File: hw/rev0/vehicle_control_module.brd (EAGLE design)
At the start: 160 x 100 mm, 455 parts, among them IC1 SJA1105TELY, IC10 TJA1100HNZ, IC11 KSZ8061MNXI-TR, IC12 TJA1100HNZ, IC14 NUP2202W1T2G, IC15 TLE9252VSKXUMA1, IC16 NUP2202W1T2G, IC17 LP5907QMFX-3.3Q1, IC2 ATSAMV71Q21B-AABT, IC3 TJA1100HNZ, IC4 FT2232HL, IC5 TRS3232EQPWRQ1, IC6 SST26VF032BT-104I_SM, IC7 DS3231SN#, IC8 TLE9252VSKXUMA1, IC9 TPS62242DRVR, J10 5-2337992-3, J11 2301843-1, J12 1017505, J13 2301843-1, J15 693022010811, J2 2305018-2, J27 2041119-2, J3 1017505, J4 1017505, J5 1017505, J6 1017505, J7 1017505, J8 1017505, J9 1017505, U1 122-2920-GR, U2 LM63625, U3 TPS62007-Q1_DGS_10, Y1 NX3225SA-25MHZ-EXS00A-CS11338, Y2 NX2016SA-25.000M-STD-CZS-1, Y3 ABM8AIG-12.000MHZ-1Z-T

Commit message: Swap to simple CAN transciever, no wake on CAN functionality required
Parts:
- removed IC15, IC8: TLE9252VSKXUMA1, samacsys:SOIC127P599X173-14N
- added C146, C147: 100nF, rcl:C0603
- added IC13, IC18: TLE9250XSJXUMA1, samacsys:SOIC127P602X173-8N
- added R195, R196: 10k, rcl:R0603
- C92, C95: value 100nF -> 10uF
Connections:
- removed net CAN0_EN: IC2.37, IC8.6
- removed net CAN0_ERR: IC2.39, IC8.8
- removed net CAN0_STBY: IC2.38, IC8.14
- removed net CAN1_EN: IC15.6, IC2.94
- removed net CAN1_ERR: IC15.8, IC2.90
- removed net CAN1_STBY: IC15.14, IC2.93
- new net CAN0_RW_MODE: IC13.8, IC2.35, R196.2
- new net CAN1_RW_MODE: IC18.8, IC2.93, R195.2
- net +3V3: now also C146.1, C147.1, IC13.5, IC18.5, R195.1, R196.1; no longer C91.1, C92.1, C94.1, C95.1, IC15.3, IC15.5, IC8.3, IC8.5
- net +5V: now also C91.1, C92.1, C94.1, C95.1, IC13.3, IC18.3
- net CAN0_H: now also IC13.7; no longer IC8.13
- net CAN0_L: now also IC13.6; no longer IC8.12
- net CAN0_RX: now also IC13.4; no longer IC8.4
- net CAN0_TX: now also IC13.1; no longer IC8.1
- net CAN1_H: now also IC18.7; no longer IC15.13
- net CAN1_L: now also IC18.6; no longer IC15.12
- net CAN1_RX: now also IC18.4; no longer IC15.4
- net CAN1_TX: now also IC18.1; no longer IC15.1
- net GND: now also C146.2, C147.2, IC13.2, IC18.2; no longer IC15.2, IC8.2
- net VBATT_PROT: no longer IC15.10, IC15.9, IC8.10, IC8.9

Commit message: Add digital inputs, connect MCU power supply
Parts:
- removed C30, C31: 8pF, rcl:C0603
- removed IC14, IC16: NUP2202W1T2G, samacsys:SOT65P210X110-6N
- removed R183, R188, R193: 1k, rcl:R0603
- removed Y2: NX2016SA-25.000M-STD-CZS-1, samacsys:NX2016SA32MEXS00ACS06465
- added C148, C149, C150, C151, C152, C153, C154, C155: 0.01uF, rcl:C0603
- added C156, C157, C158, C159, C160, C161, C163, C164, C166, C167, C168, C169, C170, C171, C172: 100nF, rcl:C0603
- added C162: 1uF, rcl:C0603
- added C165: 4.7uF, rcl:C0603
- added D28, D29, D30, D31, D32, D33, D34, D35: BAT54SWFILMY, samacsys:SOT65P210X110-3N
- added IC8: 74HC7541D-Q100J, samacsys:SOIC127P1032X265-20N
- added R198: 4.7k, rcl:R0603
- R109, R118, R128, R138, R148, R158, R168, R178: value 1k -> 100k
- R113, R123, R133, R143, R153, R163, R173: value 1k -> 4.7k
- moved R113 315.0 mm to (-294.6, 749.3)
- moved R118 283.4 mm to (-288.3, 749.3)
- moved R123 266.5 mm to (-294.6, 763.3)
- moved R128 234.2 mm to (-288.3, 763.3)
- moved R148 209.8 mm to (-280.7, 791.2)
- moved R143 207.3 mm to (-287.0, 791.2)
- moved R133 201.4 mm to (-294.6, 777.2)
- moved R138 191.2 mm to (-288.3, 777.2)
- moved R178 157.7 mm to (-288.3, 801.4)
- moved R158 154.6 mm to (-288.3, 796.3)
- moved R173 151.6 mm to (-294.6, 801.4)
- moved R153 148.9 mm to (-294.6, 796.3)
- moved R168 134.0 mm to (-275.6, 796.3)
- moved R163 131.8 mm to (-281.9, 796.3)
- moved R109 71.2 mm to (-294.6, -1394.5)
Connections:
- removed net N$22: C31.1, IC11.1, Y2.3
- removed net N$23: C30.1, IC11.2, Y2.1
- new net EXT_DINPUT_0: R198.1
- new net EXT_DINPUT_1: R113.1
- new net EXT_DINPUT_2: R123.1
- new net EXT_DINPUT_3: R133.1
- new net EXT_DINPUT_4: R143.1
- new net EXT_DINPUT_5: R153.1
- new net EXT_DINPUT_6: R163.1
- new net EXT_DINPUT_7: R173.1
- new net INTREG_1V2: C156.1, C157.1, C158.1, C159.1, C160.1, C161.1, C162.1, C163.1, C164.1, IC2.107, IC2.123, IC2.139, IC2.29, IC2.3, IC2.33, IC2.50, IC2.81
- new net N$148: C148.1, D29.3, IC8.3, R113.2, R118.2
- new net N$149: C149.1, D30.3, IC8.4, R123.2, R128.2
- new net N$150: C150.1, D31.3, IC8.5, R133.2, R138.2
- new net N$151: C151.1, D28.3, IC8.2, R109.2, R198.2
- new net N$152: C152.1, D32.3, IC8.6, R143.2, R148.2
- new net N$153: C153.1, D33.3, IC8.7, R153.2, R158.2
- new net N$154: C154.1, D34.3, IC8.8, R163.2, R168.2
- new net N$155: C155.1, D35.3, IC8.9, R173.2, R178.2
- new net PROT_DINPUT_0: IC2.108, IC8.18
- new net PROT_DINPUT_1: IC2.106, IC8.17
- new net PROT_DINPUT_2: IC2.103, IC8.16
- new net PROT_DINPUT_3: IC2.101, IC8.15
- new net PROT_DINPUT_4: IC2.100, IC8.14
- new net PROT_DINPUT_5: IC2.99, IC8.13
- new net PROT_DINPUT_6: IC2.97, IC8.12
- new net PROT_DINPUT_7: IC2.94, IC8.11
- new net SWITCH_REF_CLK: IC1.H1, IC11.1
- net +3V3: now also C165.1, C166.1, C167.1, C168.1, C169.1, C170.1, C171.1, C172.1, D28.1, D29.1, D30.1, D31.1, D32.1, D33.1, D34.1, D35.1, IC1.D10, IC1.D11, IC1.D4, IC1.D5, IC1.D7, IC1.D8, IC1.E11, IC1.E4, IC1.G11, IC1.G4, IC1.H4, IC1.K11, IC1.L10, IC1.L11, IC1.L5, IC1.L8, IC2.134, IC2.143, IC2.30, IC2.43, IC2.5, IC2.72, IC2.80, IC2.96, IC8.20; no longer IC14.5, IC16.5
- net 3V3_AD_REF: now also IC2.9
- net CAN0_H: no longer IC14.1
- net CAN0_L: no longer IC14.6
- net CAN0_RW_MODE: now also IC2.37; no longer IC2.35
- net CAN1_H: no longer IC16.1
- net CAN1_L: no longer IC16.6
- net CAN1_RW_MODE: now also IC2.90; no longer IC2.93
- net GND: now also C148.2, C149.2, C150.2, C151.2, C152.2, C153.2, C154.2, C155.2, C156.2, C157.2, C158.2, C159.2, C160.2, C161.2, C162.2, C163.2, C164.2, C165.2, C166.2, C167.2, C168.2, C169.2, C170.2, C171.2, C172.2, D28.2, D29.2, D30.2, D31.2, D32.2, D33.2, D34.2, D35.2, IC1.J2, IC1.L2, IC1.N13, IC1.P1, IC2.8, IC8.1, IC8.10, IC8.19, R109.1, R118.1, R128.1, R138.1, R148.1, R158.1, R168.1, R178.1; no longer C112.2, C113.2, C115.2, C117.2, C119.2, C121.2, C123.2, C125.2, C127.2, C129.2, C131.2, C133.2, C135.2, C137.2, C139.2, C141.2, C143.2, C145.2, C30.2, C31.2, IC14.2, IC16.2, R109.2, R113.2, R118.2, R123.2, R128.2, R133.2, R138.2, R143.2, R148.2, R153.2, R158.2, R163.2, R168.2, R173.2, R178.2, R183.2, R188.2, R193.2, Y2.2, Y2.4
- net HIGHSIDE_0_EN: now also IC2.98
- net HIGHSIDE_10_EN: now also IC2.39
- net HIGHSIDE_11_EN: now also IC2.40
- net HIGHSIDE_12_EN: now also IC2.45
- net HIGHSIDE_13_EN: now also IC2.47
- net HIGHSIDE_14_EN: now also IC2.48
- net HIGHSIDE_15_EN: now also IC2.49
- net HIGHSIDE_16_EN: now also IC2.54
- net HIGHSIDE_17_EN: now also IC2.55
- net HIGHSIDE_1_EN: now also IC2.93
- net HIGHSIDE_2_EN: now also IC2.59
- net HIGHSIDE_3_EN: now also IC2.35
- net HIGHSIDE_4_EN: now also IC2.118
- net HIGHSIDE_5_EN: now also IC2.36
- net HIGHSIDE_6_EN: now also IC2.46
- net HIGHSIDE_7_EN: now also IC2.6
- net HIGHSIDE_8_EN: now also IC2.7
- net HIGHSIDE_9_EN: now also IC2.38
- net N$100: now also C115.2
- net N$102: no longer R118.1
- net N$103: now also C117.2
- net N$105: no longer R123.1
- net N$106: now also C119.2
- net N$108: no longer R128.1
- net N$109: now also C121.2
- net N$111: no longer R133.1
- net N$112: now also C123.2
- net N$114: no longer R138.1
- net N$115: now also C125.2
- net N$117: no longer R143.1
- net N$118: now also C127.2
- net N$120: no longer R148.1
- net N$121: now also C129.2
- net N$123: no longer R153.1
- net N$124: now also C131.2
- net N$126: no longer R158.1
- net N$127: now also C133.2
- net N$129: no longer R163.1
- net N$130: now also C135.2
- net N$132: no longer R168.1
- net N$133: now also C137.2
- net N$135: no longer R173.1
- net N$136: now also C139.2
- net N$138: no longer R178.1
- net N$139: now also C141.2
- net N$141: no longer R183.1
- net N$142: now also C143.2
- net N$144: no longer R188.1
- net N$145: now also C145.2
- net N$147: no longer R193.1
- net N$94: now also C112.2
- net N$96: now also C113.2
- net N$97: no longer R109.1
- net N$99: no longer R113.1
- net VDD: now also IC1.D6, IC1.D9, IC1.F11, IC1.F4, IC1.J1, IC1.J11, IC1.J4, IC1.K1, IC1.L6, IC1.L9

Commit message: Fix connection between MCU and switch
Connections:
- removed net RMII0_RXER: IC1.H2, IC2.119
- new net RMII0_TXER: IC1.A3, IC2.119
- net RMII0_CRSDV: now also IC2.132; no longer IC2.126
- net RMII0_RXD0: now also IC2.131; no longer IC2.125
- net RMII0_RXD1: now also IC2.128; no longer IC2.121
- net RMII0_TXD0: now also IC2.125; no longer IC2.131
- net RMII0_TXD1: now also IC2.121; no longer IC2.128
- net RMII0_TXEN: now also IC2.126; no longer IC2.132
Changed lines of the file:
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@@
 <wire x1="1.962" y1="-3.95" x2="17.66" y2="33.28" width="0" layer="19" extent="1-1"/>
 </signal>
-<signal name="RMII0_RXER">
-<contactref element="IC2" pad="119"/>
-<contactref element="IC1" pad="H2"/>
-<wire x1="16.45" y1="-1.962" x2="18.46" y2="30.08" width="0" layer="19" extent="1-1"/>
-</signal>
 <signal name="RMII0_RXD1">
+<contactref element="IC1" pad="F2"/>
+<contactref element="IC2" pad="128"/>
+<wire x1="11.95" y1="-1.962" x2="18.46" y2="31.68" width="0" layer="19" extent="1-1"/>
+</signal>
+<signal name="RMII0_RXD0">
+<contactref element="IC1" pad="E1"/>
+<contactref element="IC2" pad="131"/>
+<wire x1="10.45" y1="-1.962" x2="17.66" y2="32.48" width="0" layer="19" extent="1-1"/>
+</signal>
+<signal name="RMII0_CRSDV">
+<contactref element="IC1" pad="G1"/>
+<contactref element="IC2" pad="132"/>
+<wire x1="9.95" y1="-1.962" x2="17.66" y2="30.88" width="0" layer="19" extent="1-1"/>
+</signal>
+<signal name="RMII0_TXD1">
+<contactref element="IC1" pad="B1"/>
 <contactref element="IC2" pad="121"/>
-<contactref element="IC1" pad="F2"/>
-<wire x1="15.45" y1="-1.962" x2="18.46" y2="31.68" width="0" layer="19" extent="1-1"/>
-</signal>
-<signal name="RMII0_RXD0">
+<wire x1="15.45" y1="-1.962" x2="17.66" y2="34.88" width="0" layer="19" extent="1-1"/>
+</signal>
+<signal name="RMII0_TXD0">
+<contactref element="IC1" pad="A2"/>
 <contactref element="IC2" pad="125"/>
-<contactref element="IC1" pad="E1"/>
-<wire x1="13.45" y1="-1.962" x2="17.66" y2="32.48" width="0" layer="19" extent="1-1"/>
-</signal>
-<signal name="RMII0_CRSDV">
+<wire x1="13.45" y1="-1.962" x2="18.46" y2="35.68" width="0" layer="19" extent="1-1"/>
+</signal>
+<signal name="RMII0_TXEN">
+<contactref element="IC1" pad="D2"/>
 <contactref element="IC2" pad="126"/>
-<contactref element="IC1" pad="G1"/>
-<wire x1="12.95" y1="-1.962" x2="17.66" y2="30.88" width="0" layer="19" extent="1-1"/>
-</signal>
-<signal name="RMII0_TXD1">
-<contactref element="IC2" pad="128"/>
-<contactref element="IC1" pad="B1"/>
-<wire x1="11.95" y1="-1.962" x2="17.66" y2="34.88" width="0" layer="19" extent="1-1"/>
-</signal>
-<signal name="RMII0_TXD0">
-<contactref element="IC2" pad="131"/>
-<contactref element="IC1" pad="A2"/>
-<wire x1="10.45" y1="-1.962" x2="18.46" y2="35.68" width="0" layer="19" extent="1-1"/>
-</signal>
-<signal name="RMII0_TXEN">
-<contactref element="IC2" pad="132"/>
-<contactref element="IC1" pad="D2"/>
-<wire x1="9.95" y1="-1.962" x2="18.46" y2="33.28" width="0" layer="19" extent="1-1"/>
+<wire x1="12.95" y1="-1.962" x2="18.46" y2="33.28" width="0" layer="19" extent="1-1"/>
 </signal>
 <signal name="I2C0_TWCK">
@@
 <wire x1="23.438" y1="-17.45" x2="23.438" y2="-4.45" width="0" layer="19" extent="1-1"/>
 </signal>
+<signal name="RMII0_TXER">
+<contactref element="IC1" pad="A3"/>
+<contactref element="IC2" pad="119"/>
+<wire x1="16.45" y1="-1.962" x2="19.26" y2="35.68" width="0" layer="19" extent="1-1"/>
+</signal>
 </signals>

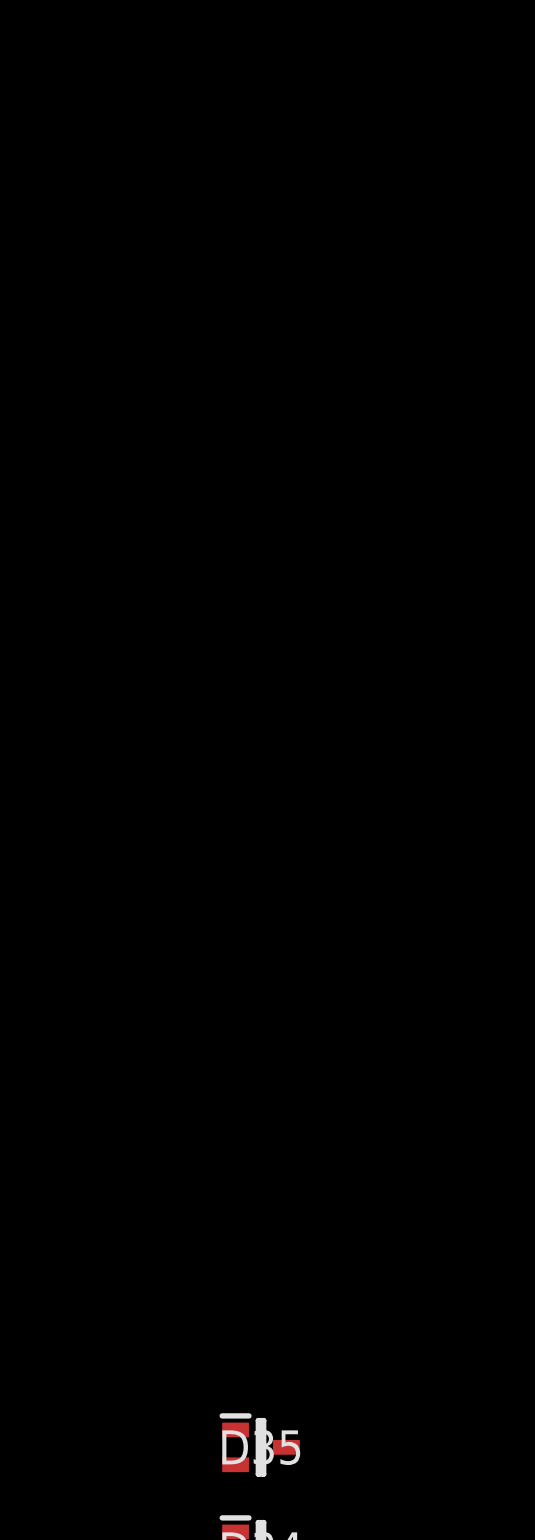
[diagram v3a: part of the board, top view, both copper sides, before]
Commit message: Add Debug LEDs
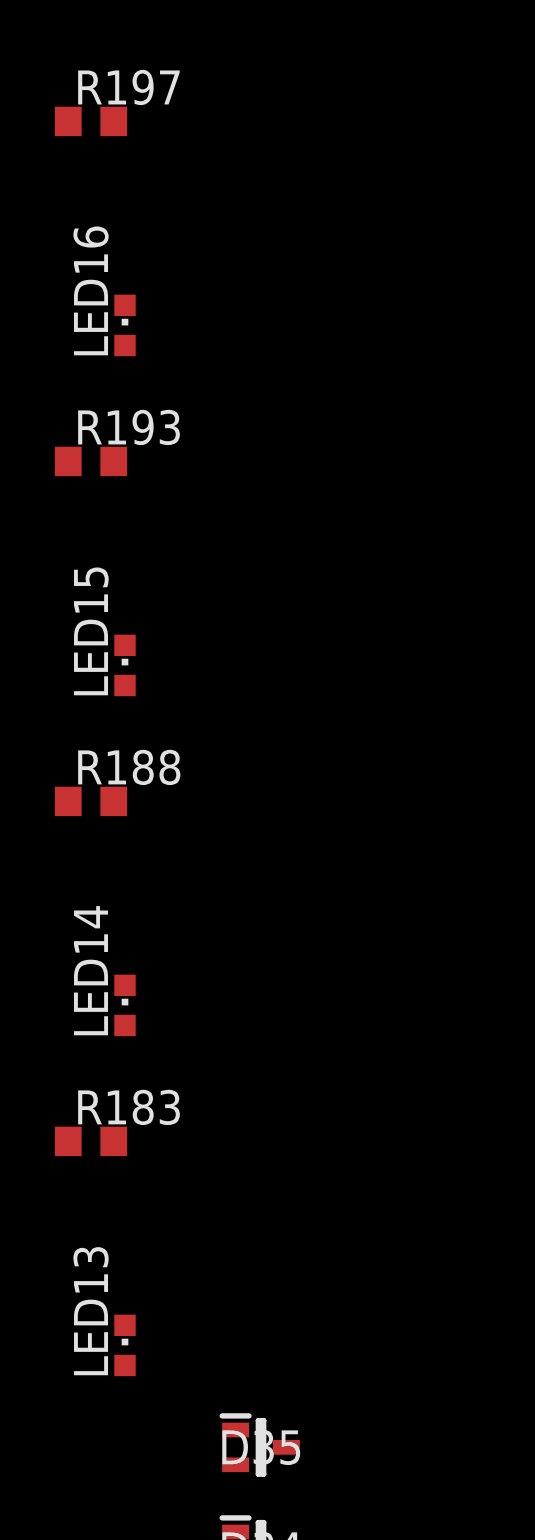
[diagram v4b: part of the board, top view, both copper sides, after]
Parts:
- added LED13, LED14, LED15, LED16: (no value), led:CHIPLED_0603
- added R183, R188, R193, R197: 10k, rcl:R0603
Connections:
- new net DEBUG_LED0: IC2.117, R183.1
- new net DEBUG_LED1: IC2.116, R188.1
- new net DEBUG_LED2: IC2.112, R193.1
- new net DEBUG_LED3: IC2.111, R197.1
- new net N$156: LED15.A, R193.2
- new net N$157: LED16.A, R197.2
- new net N$22: LED13.A, R183.2
- new net N$23: LED14.A, R188.2
- net GND: now also LED13.C, LED14.C, LED15.C, LED16.C
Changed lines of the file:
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@@
 <attribute name="VALUE" x="-295.275" y="-1482.725" size="1.27" layer="27"/>
 </element>
+<element name="R183" library="rcl" library_urn="urn:adsk.eagle:library:334" package="R0603" package3d_urn="urn:adsk.eagle:package:23555/3" value="10k" x="-294.64" y="829.31" smashed="yes">
+<attribute name="NAME" x="-295.275" y="829.945" size="1.27" layer="25"/>
+<attribute name="POPULARITY" value="77" x="-294.64" y="-1485.9" size="1.778" layer="27" display="off"/>
+<attribute name="SPICEPREFIX" value="R" x="-294.64" y="-1485.9" size="1.778" layer="27" display="off"/>
+<attribute name="VALUE" x="-295.275" y="827.405" size="1.27" layer="27"/>
+</element>
+<element name="LED13" library="led" library_urn="urn:adsk.eagle:library:259" package="CHIPLED_0603" package3d_urn="urn:adsk.eagle:package:15822/2" value="" x="-293.37" y="821.69" smashed="yes">
+<attribute name="NAME" x="-294.005" y="820.42" size="1.27" layer="25" rot="R90"/>
+<attribute name="POPULARITY" value="28" x="-299.72" y="-1485.9" size="1.778" layer="27" display="off"/>
+<attribute name="VALUE" x="-291.465" y="820.42" size="1.27" layer="27" rot="R90"/>
+</element>
+<element name="R188" library="rcl" library_urn="urn:adsk.eagle:library:334" package="R0603" package3d_urn="urn:adsk.eagle:package:23555/3" value="10k" x="-294.64" y="842.01" smashed="yes">
+<attribute name="NAME" x="-295.275" y="842.645" size="1.27" layer="25"/>
+<attribute name="POPULARITY" value="77" x="-294.64" y="-1485.9" size="1.778" layer="27" display="off"/>
+<attribute name="SPICEPREFIX" value="R" x="-294.64" y="-1485.9" size="1.778" layer="27" display="off"/>
+<attribute name="VALUE" x="-295.275" y="840.105" size="1.27" layer="27"/>
+</element>
+<element name="LED14" library="led" library_urn="urn:adsk.eagle:library:259" package="CHIPLED_0603" package3d_urn="urn:adsk.eagle:package:15822/2" value="" x="-293.37" y="834.39" smashed="yes">
+<attribute name="NAME" x="-294.005" y="833.12" size="1.27" layer="25" rot="R90"/>
+<attribute name="POPULARITY" value="28" x="-299.72" y="-1485.9" size="1.778" layer="27" display="off"/>
+<attribute name="VALUE" x="-291.465" y="833.12" size="1.27" layer="27" rot="R90"/>
+</element>
+<element name="R193" library="rcl" library_urn="urn:adsk.eagle:library:334" package="R0603" package3d_urn="urn:adsk.eagle:package:23555/3" value="10k" x="-294.64" y="854.71" smashed="yes">
+<attribute name="NAME" x="-295.275" y="855.345" size="1.27" layer="25"/>
+<attribute name="POPULARITY" value="77" x="-294.64" y="-1485.9" size="1.778" layer="27" display="off"/>
+<attribute name="SPICEPREFIX" value="R" x="-294.64" y="-1485.9" size="1.778" layer="27" display="off"/>
+<attribute name="VALUE" x="-295.275" y="852.805" size="1.27" layer="27"/>
+</element>
+<element name="LED15" library="led" library_urn="urn:adsk.eagle:library:259" package="CHIPLED_0603" package3d_urn="urn:adsk.eagle:package:15822/2" value="" x="-293.37" y="847.09" smashed="yes">
+<attribute name="NAME" x="-294.005" y="845.82" size="1.27" layer="25" rot="R90"/>
+<attribute name="POPULARITY" value="28" x="-299.72" y="-1485.9" size="1.778" layer="27" display="off"/>
+<attribute name="VALUE" x="-291.465" y="845.82" size="1.27" layer="27" rot="R90"/>
+</element>
+<element name="R197" library="rcl" library_urn="urn:adsk.eagle:library:334" package="R0603" package3d_urn="urn:adsk.eagle:package:23555/3" value="10k" x="-294.64" y="867.41" smashed="yes">
+<attribute name="NAME" x="-295.275" y="868.045" size="1.27" layer="25"/>
+<attribute name="POPULARITY" value="77" x="-294.64" y="-1485.9" size="1.778" layer="27" display="off"/>
+<attribute name="SPICEPREFIX" value="R" x="-294.64" y="-1485.9" size="1.778" layer="27" display="off"/>
+<attribute name="VALUE" x="-295.275" y="865.505" size="1.27" layer="27"/>
+</element>
+<element name="LED16" library="led" library_urn="urn:adsk.eagle:library:259" package="CHIPLED_0603" package3d_urn="urn:adsk.eagle:package:15822/2" value="" x="-293.37" y="859.79" smashed="yes">
+<attribute name="NAME" x="-294.005" y="858.52" size="1.27" layer="25" rot="R90"/>
+<attribute name="POPULARITY" value="28" x="-299.72" y="-1485.9" size="1.778" layer="27" display="off"/>
+<attribute name="VALUE" x="-291.465" y="858.52" size="1.27" layer="27" rot="R90"/>
+</element>
 </elements>
 <signals>
@@
 <contactref element="IC1" pad="J2"/>
 <contactref element="IC1" pad="N13"/>
+<contactref element="LED13" pad="C"/>
+<contactref element="LED14" pad="C"/>
+<contactref element="LED15" pad="C"/>
+<contactref element="LED16" pad="C"/>
 <wire x1="-293.79" y1="-1475.74" x2="-293.79" y2="-1480.82" width="0" layer="19" extent="1-1"/>
 <wire x1="-293.79" y1="-1470.66" x2="-293.79" y2="-1475.74" width="0" layer="19" extent="1-1"/>
@@
 <wire x1="-289.24" y1="813.42" x2="-289.24" y2="809.61" width="0" layer="19" extent="1-1"/>
 <wire x1="-289.24" y1="817.23" x2="-289.24" y2="813.42" width="0" layer="19" extent="1-1"/>
+<wire x1="-293.37" y1="822.44" x2="-289.24" y2="817.23" width="0" layer="19" extent="1-1"/>
 <wire x1="-276.44" y1="796.29" x2="-281.52" y2="791.21" width="0" layer="19" extent="1-1"/>
+<wire x1="-293.37" y1="835.14" x2="-293.37" y2="822.44" width="0" layer="19" extent="1-1"/>
+<wire x1="-293.37" y1="847.84" x2="-293.37" y2="835.14" width="0" layer="19" extent="1-1"/>
+<wire x1="-293.37" y1="860.54" x2="-293.37" y2="847.84" width="0" layer="19" extent="1-1"/>
 </signal>
 <signal name="ADC0_10">
@@
 <wire x1="16.45" y1="-1.962" x2="19.26" y2="35.68" width="0" layer="19" extent="1-1"/>
 </signal>
+<signal name="N$22">
+<contactref element="R183" pad="2"/>
+<contactref element="LED13" pad="A"/>
+<wire x1="-293.37" y1="820.94" x2="-293.79" y2="829.31" width="0" layer="19" extent="1-1"/>
+</signal>
+<signal name="DEBUG_LED0">
+<contactref element="R183" pad="1"/>
+<contactref element="IC2" pad="117"/>
+<wire x1="17.45" y1="-1.962" x2="-295.49" y2="829.31" width="0" layer="19" extent="1-1"/>
+</signal>
+<signal name="N$23">
+<contactref element="R188" pad="2"/>
+<contactref element="LED14" pad="A"/>
+<wire x1="-293.37" y1="833.64" x2="-293.79" y2="842.01" width="0" layer="19" extent="1-1"/>
+</signal>
+<signal name="N$156">
+<contactref element="R193" pad="2"/>
+<contactref element="LED15" pad="A"/>
+<wire x1="-293.37" y1="846.34" x2="-293.79" y2="854.71" width="0" layer="19" extent="1-1"/>
+</signal>
+<signal name="N$157">
+<contactref element="R197" pad="2"/>
+<contactref element="LED16" pad="A"/>
+<wire x1="-293.37" y1="859.04" x2="-293.79" y2="867.41" width="0" layer="19" extent="1-1"/>
+</signal>
+<signal name="DEBUG_LED1">
+<contactref element="R188" pad="1"/>
+<contactref element="IC2" pad="116"/>
+<wire x1="17.95" y1="-1.962" x2="-295.49" y2="842.01" width="0" layer="19" extent="1-1"/>
+</signal>
+<signal name="DEBUG_LED2">
+<contactref element="R193" pad="1"/>
+<contactref element="IC2" pad="112"/>
+<wire x1="19.95" y1="-1.962" x2="-295.49" y2="854.71" width="0" layer="19" extent="1-1"/>
+</signal>
+<signal name="DEBUG_LED3">
+<contactref element="R197" pad="1"/>
+<contactref element="IC2" pad="111"/>
+<wire x1="20.45" y1="-1.962" x2="-295.49" y2="867.41" width="0" layer="19" extent="1-1"/>
+</signal>
 </signals>
